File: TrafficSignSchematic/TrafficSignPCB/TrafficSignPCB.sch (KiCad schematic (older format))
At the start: 32 parts, among them J1 IDC connector, J2 3.96mm pitch 4-pin polarized 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, J3 Power In, U1 ATmega328P-PU, U2 SIM800L, Y1 16MHz

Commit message: Forgot to save...
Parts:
- D1, D2: footprint Diode_THT:D_DO-27_P15.24mm_Horizontal -> Diode_THT:D_DO-27_P12.70mm_Horizontal
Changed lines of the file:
@@
 F 0 "D1" V 9204 3279 50  0000 L CNN
 F 1 "100V/5A" V 9295 3279 50  0000 L CNN
-F 2 "Diode_THT:D_DO-27_P15.24mm_Horizontal" H 9250 3200 50  0001 C CNN
+F 2 "Diode_THT:D_DO-27_P12.70mm_Horizontal" H 9250 3200 50  0001 C CNN
 F 3 "https://store.comet.bg/Catalogue/Product/9381/" H 9250 3200 50  0001 C CNN
 	1    9250 3200
@@
 F 0 "D2" V 9204 5029 50  0000 L CNN
 F 1 "100V/5A" V 9295 5029 50  0000 L CNN
-F 2 "Diode_THT:D_DO-27_P15.24mm_Horizontal" H 9250 4950 50  0001 C CNN
+F 2 "Diode_THT:D_DO-27_P12.70mm_Horizontal" H 9250 4950 50  0001 C CNN
 F 3 "https://store.comet.bg/Catalogue/Product/9381/" H 9250 4950 50  0001 C CNN
 	1    9250 4950

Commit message: Moving elements
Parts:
- added H1, H2, H3, H4: MountingHole, MountingHole:MountingHole_3.2mm_M3_ISO14580, symbol Mechanical:MountingHole
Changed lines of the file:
@@
 Wire Wire Line
 	10350 5150 10650 5150
+$Comp
+L Mechanical:MountingHole H1
+U 1 1 5E2BE7C8
+P 4800 5550
+F 0 "H1" H 4900 5596 50  0000 L CNN
+F 1 "MountingHole" H 4900 5505 50  0000 L CNN
+F 2 "MountingHole:MountingHole_3.2mm_M3_ISO14580" H 4800 5550 50  0001 C CNN
+F 3 "~" H 4800 5550 50  0001 C CNN
+	1    4800 5550
+	1    0    0    -1
+$EndComp
+$Comp
+L Mechanical:MountingHole H2
+U 1 1 5E2BF783
+P 4800 5750
+F 0 "H2" H 4900 5796 50  0000 L CNN
+F 1 "MountingHole" H 4900 5705 50  0000 L CNN
+F 2 "MountingHole:MountingHole_3.2mm_M3_ISO14580" H 4800 5750 50  0001 C CNN
+F 3 "~" H 4800 5750 50  0001 C CNN
+	1    4800 5750
+	1    0    0    -1
+$EndComp
+$Comp
+L Mechanical:MountingHole H3
+U 1 1 5E2CA4B3
+P 4800 5950
+F 0 "H3" H 4900 5996 50  0000 L CNN
+F 1 "MountingHole" H 4900 5905 50  0000 L CNN
+F 2 "MountingHole:MountingHole_3.2mm_M3_ISO14580" H 4800 5950 50  0001 C CNN
+F 3 "~" H 4800 5950 50  0001 C CNN
+	1    4800 5950
+	1    0    0    -1
+$EndComp
+$Comp
+L Mechanical:MountingHole H4
+U 1 1 5E2D525A
+P 4800 6150
+F 0 "H4" H 4900 6196 50  0000 L CNN
+F 1 "MountingHole" H 4900 6105 50  0000 L CNN
+F 2 "MountingHole:MountingHole_3.2mm_M3_ISO14580" H 4800 6150 50  0001 C CNN
+F 3 "~" H 4800 6150 50  0001 C CNN
+	1    4800 6150
+	1    0    0    -1
+$EndComp
 $EndSCHEMATC

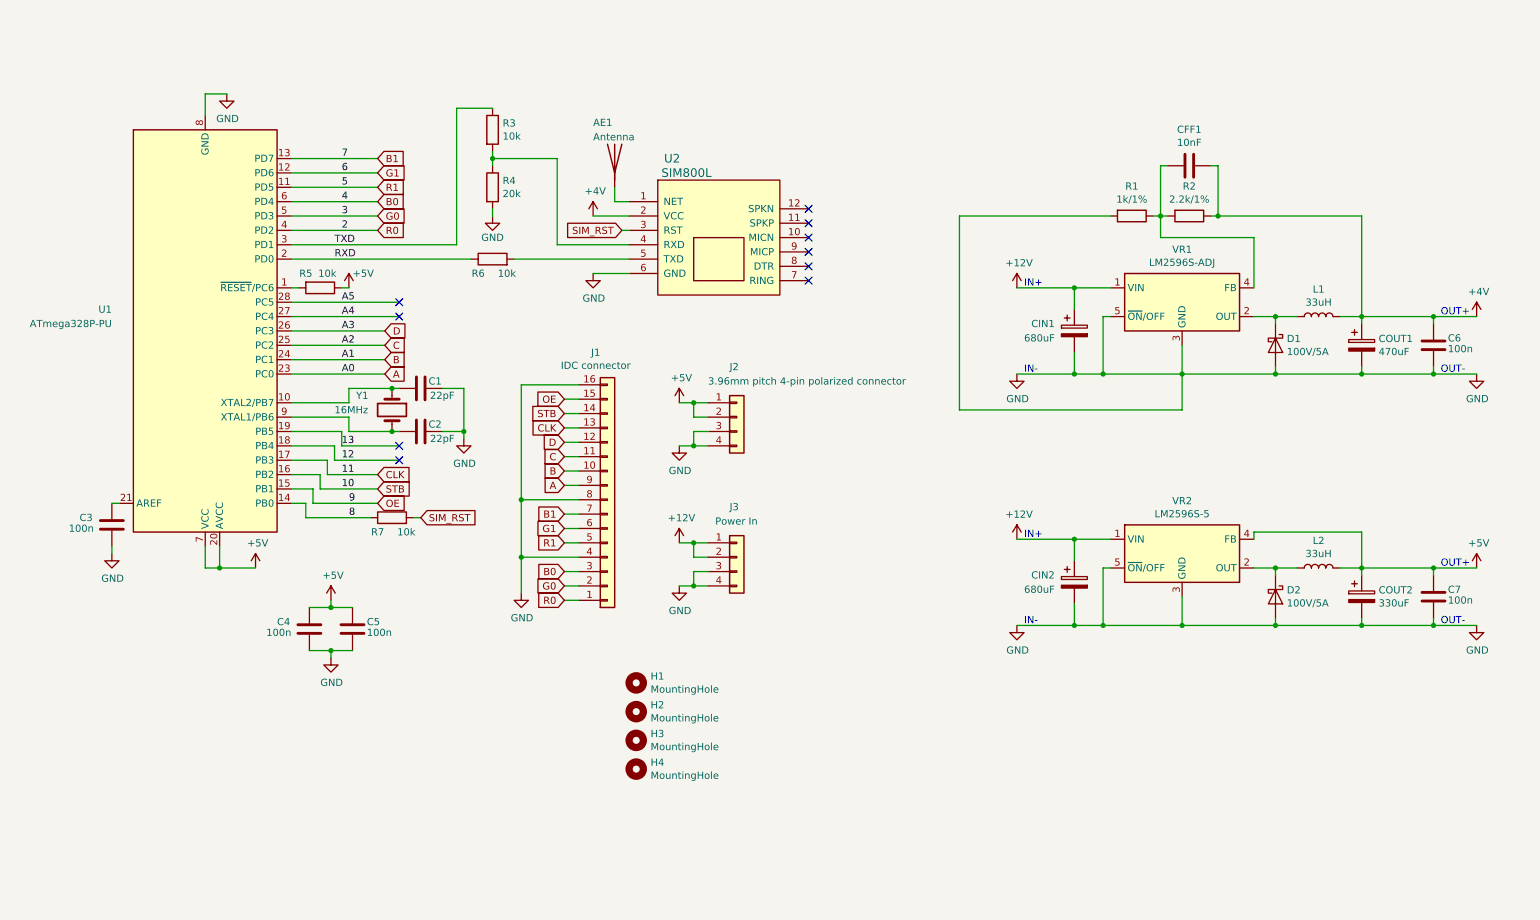
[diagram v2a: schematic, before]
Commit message: Updated the PCB schematic and layout
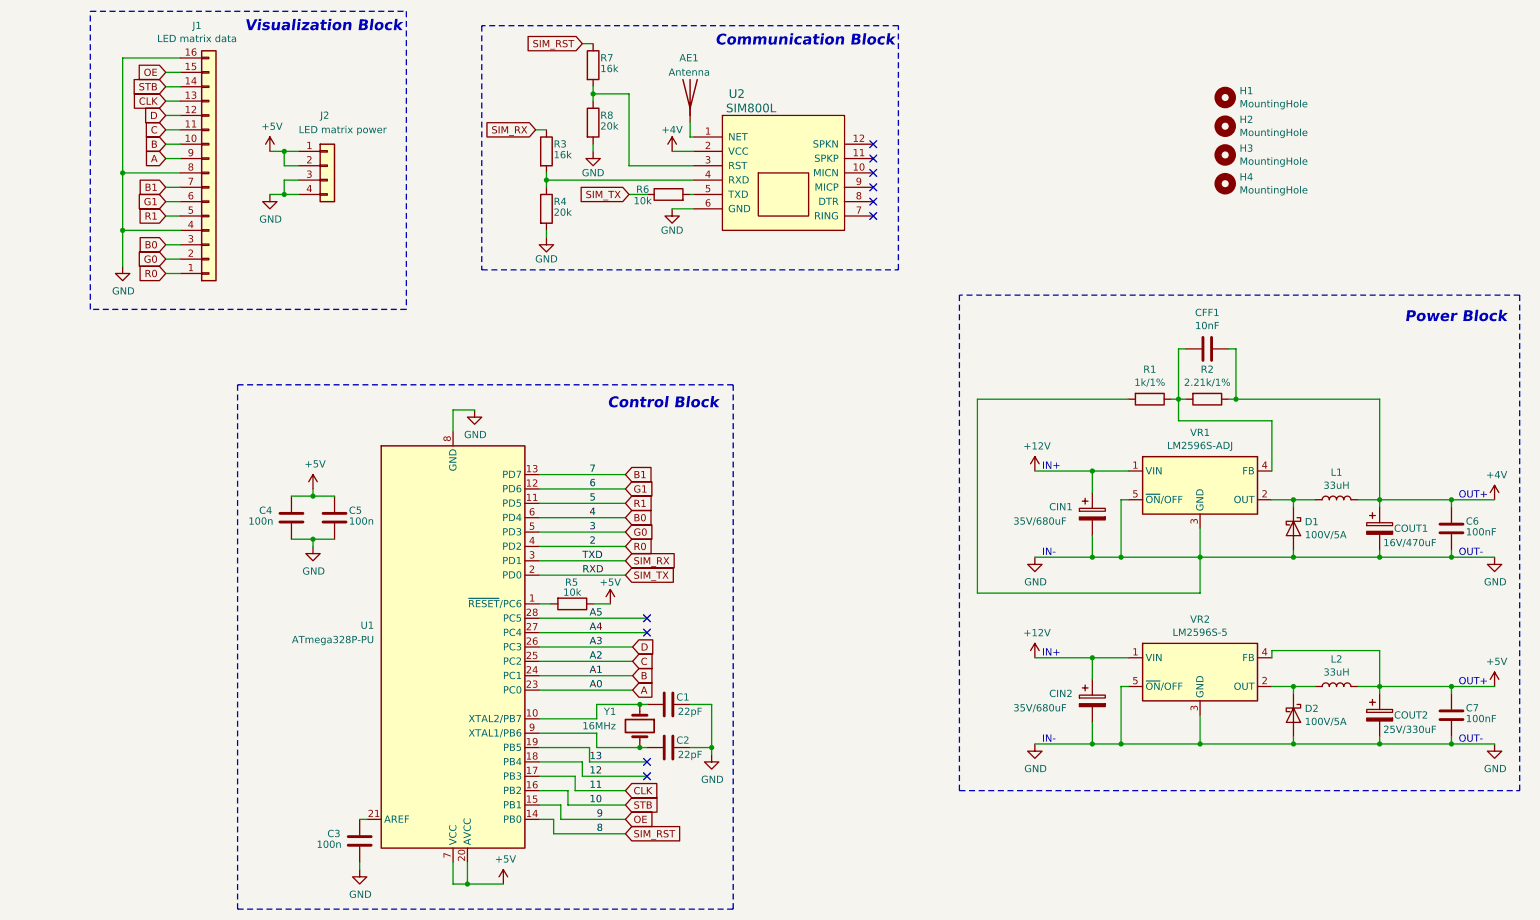
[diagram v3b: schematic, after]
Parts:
- removed J3: Power In, Connector_Molex:Molex_KK-396_A-41791-0004_1x04_P3.96mm_Vertical, symbol Connector_Generic:Conn_01x04
- added R8: 20k, Resistor_THT:R_Axial_DIN0204_L3.6mm_D1.6mm_P7.62mm_Horizontal, symbol Device:R
- C6, C7: value 100n -> 100nF
- CIN1, CIN2: value 680uF -> 35V/680uF
- COUT1: value 470uF -> 16V/470uF
- COUT2: value 330uF -> 25V/330uF
- J1: value IDC connector -> LED matrix data
- J2: value 3.96mm pitch 4-pin polarized connector -> LED matrix power
- R2: value 2.2k/1% -> 2.21k/1%
- R3, R7: value 10k -> 16k
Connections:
- net 8 is gone; now on net SIM_RST: R7.1, U1.14 (PB0)
- net GND: now also R8.2
- net SIM_RST: no longer R7.2, U2.3 (RST)
- net RXD renamed SIM_TX
- net TXD renamed SIM_RX
- new net: R7.2, R8.1, U2.3 (RST)
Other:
- note added: "Communication Block"
- note added: "Control Block"
- note added: "Power Block"
- note added: "Visualization Block"
- moved on the sheet: AE1, C1, C2, C3, C4, C5, C6, C7, CFF1, CIN1, CIN2, COUT1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

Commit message: Made small adjustments to PCB design
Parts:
- added J3: Power In, Connector_Molex:Molex_KK-396_A-41791-0004_1x04_P3.96mm_Vertical, symbol Connector_Generic:Conn_01x04
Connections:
- net +12V: now also J3.1 (Pin_1), J3.2 (Pin_2)
- net GND: now also J3.3 (Pin_3), J3.4 (Pin_4)
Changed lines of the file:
@@
 encoding utf-8
 Sheet 1 1
-Title ""
-Date ""
-Rev ""
+Title "Traffic sign PCB schematic"
+Date "2020-02-15"
+Rev "1"
 Comp ""
 Comment1 ""
@@
 Wire Notes Line
 	7050 6300 10950 6300
-Wire Notes Line
-	10950 6300 10950 2850
-Text Notes 10150 3050 0    75   Italic 15
+Text Notes 10150 2775 0    75   Italic 15
 Power Block
 Wire Notes Line
-	10950 2850 7050 2850
+	10950 2575 7050 2575
 Wire Wire Line
 	8575 3575 8575 3225
@@
 	8575 3225 8625 3225
 Wire Notes Line
-	7050 2850 7050 6300
+	7050 2575 7050 6300
 $Comp
 L Device:R R7
@@
 Wire Wire Line
 	4750 1450 4750 1950
+Wire Notes Line
+	10950 6300 10950 2575
+$Comp
+L power:GND #PWR0124
+U 1 1 5E500F33
+P 7475 3250
+F 0 "#PWR0124" H 7475 3000 50  0001 C CNN
+F 1 "GND" H 7480 3077 50  0000 C CNN
+F 2 "" H 7475 3250 50  0001 C CNN
+F 3 "" H 7475 3250 50  0001 C CNN
+	1    7475 3250
+	1    0    0    -1
+$EndComp
+Connection ~ 7575 2950
+Wire Wire Line
+	7575 2950 7475 2950
+Wire Wire Line
+	7575 3050 7575 2950
+Connection ~ 7575 3250
+Wire Wire Line
+	7575 3250 7475 3250
+Wire Wire Line
+	7575 3150 7575 3250
+Wire Wire Line
+	7675 3250 7575 3250
+Wire Wire Line
+	7675 3150 7575 3150
+Wire Wire Line
+	7675 3050 7575 3050
+Wire Wire Line
+	7675 2950 7575 2950
+$Comp
+L Connector_Generic:Conn_01x04 J3
+U 1 1 5E500F43
+P 7875 3050
+F 0 "J3" H 7825 3400 50  0000 L CNN
+F 1 "Power In" H 7675 3300 50  0000 L CNN
+F 2 "Connector_Molex:Molex_KK-396_A-41791-0004_1x04_P3.96mm_Vertical" H 7875 3050 50  0001 C CNN
+F 3 "https://store.comet.bg/Catalogue/Product/25223/" H 7875 3050 50  0001 C CNN
+	1    7875 3050
+	1    0    0    -1
+$EndComp
+$Comp
+L power:+12V #PWR?
+U 1 1 5E568067
+P 7475 2950
+F 0 "#PWR?" H 7475 2800 50  0001 C CNN
+F 1 "+12V" H 7490 3123 50  0000 C CNN
+F 2 "" H 7475 2950 50  0001 C CNN
+F 3 "" H 7475 2950 50  0001 C CNN
+	1    7475 2950
+	1    0    0    -1
+$EndComp
 $EndSCHEMATC
